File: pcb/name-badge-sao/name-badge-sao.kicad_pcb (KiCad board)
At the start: 2 copper layers, 83.8 x 44.5 mm, 109 parts, among them J1 USB_C_Receptacle_USB2.0, J2 Conn_01x02, SW1 SW_SPDT, U1 IS31FL3731-QF, U2 SAMD21_MOD, U3 W25Q32JVSS, U4 TP4057

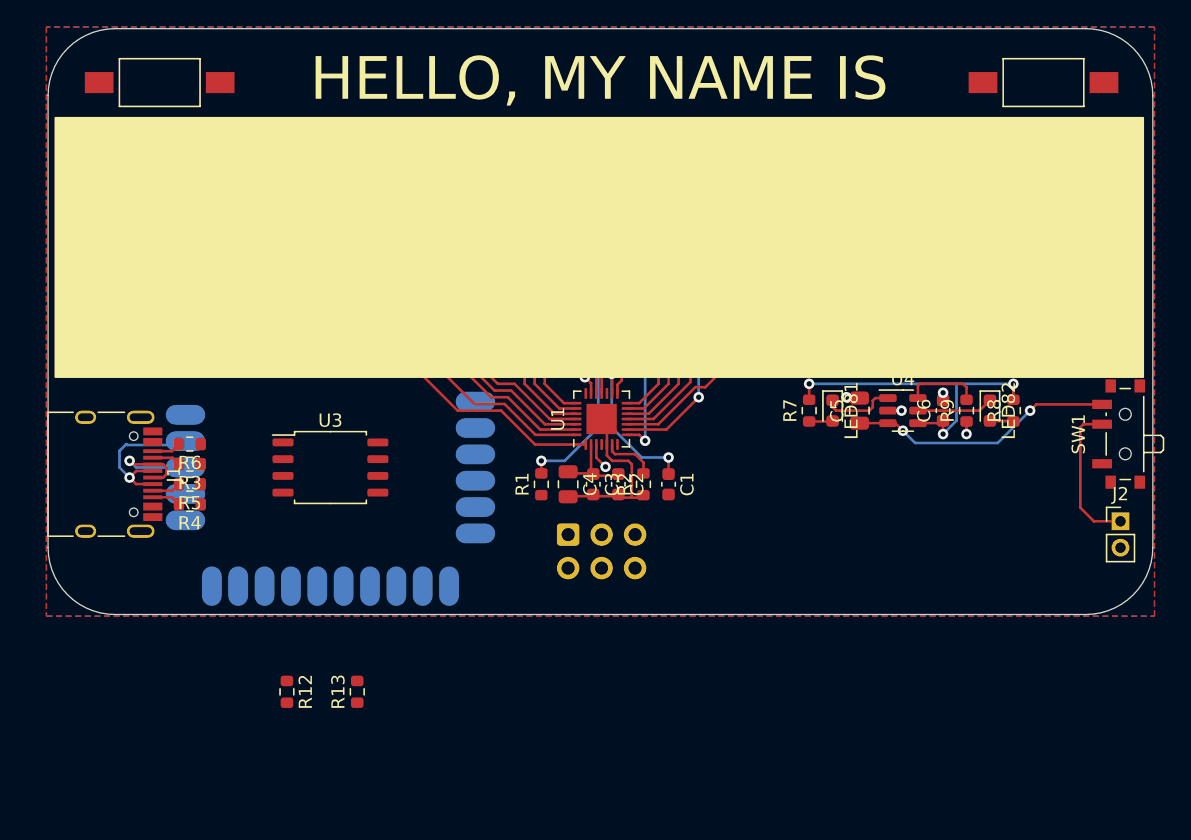
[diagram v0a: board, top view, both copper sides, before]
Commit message: Moving to an all-new circuit design (normal matrix, no charlieplexing) with a new MCU, because why not change everything?
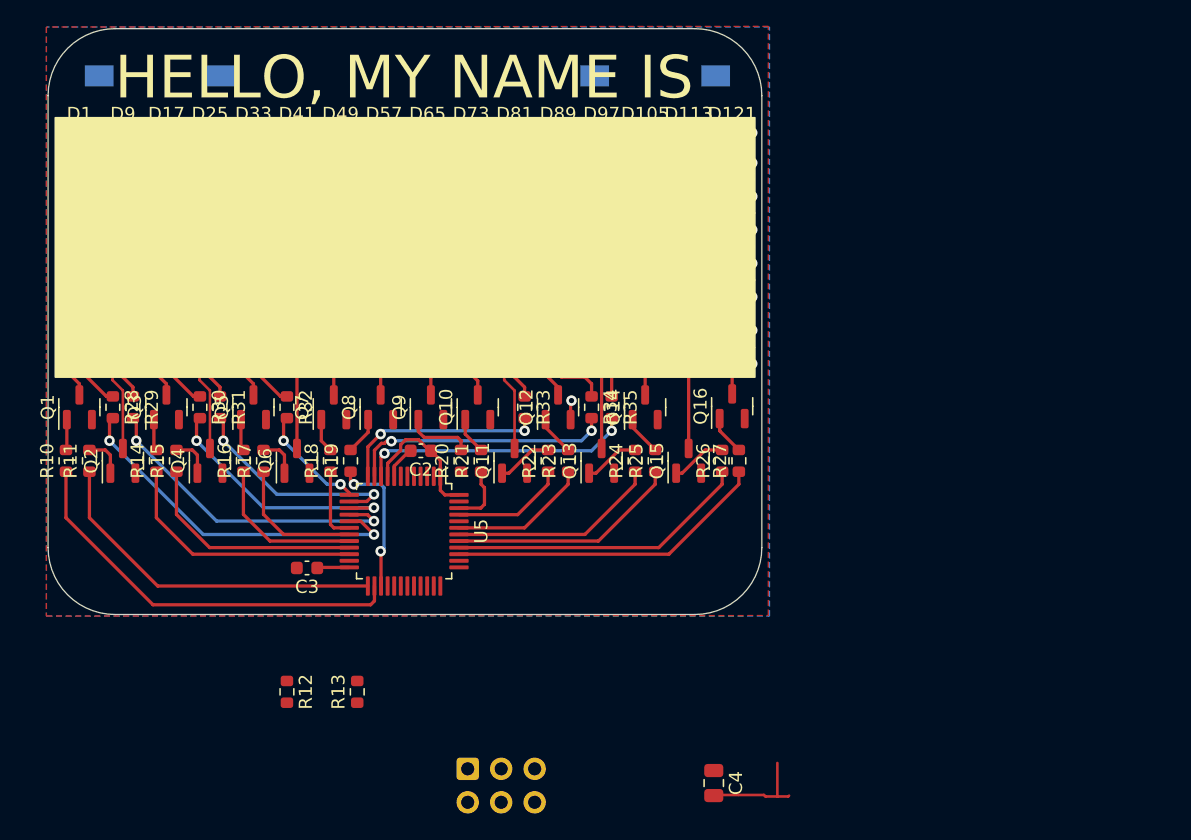
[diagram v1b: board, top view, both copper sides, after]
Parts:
- removed C1: 100n, Capacitor_SMD:C_0603_1608Metric
- removed C5: 10u, Capacitor_SMD:C_0805_2012Metric
- removed C6: 1u, Capacitor_SMD:C_0603_1608Metric
- removed J1: USB_C_Receptacle_USB2.0, Connector_USB:USB_C_Receptacle_HRO_TYPE-C-31-M-12
- removed J2: Conn_01x02, Connector_PinHeader_2.00mm:PinHeader_1x02_P2.00mm_Vertical
- removed LED1, LED10, LED11, LED12, LED13, LED14, LED15, LED16, LED17, LED18, LED19, LED2, LED20, LED21, LED22, LED23, LED24, LED25, LED26, LED27, LED28, LED29, LED3, LED30, LED31, LED32, LED33, LED34, LED35, LED36, LED37, LED38, LED39, LED4, LED40, LED41, LED42, LED43, LED44, LED45, LED46, LED47, LED48, LED49, LED5, LED50, LED51, LED52, LED53, LED54, LED55, LED56, LED57, LED58, LED59, LED6, LED60, LED61, LED62, LED63, LED64, LED65, LED66, LED67, LED68, LED69, LED7, LED70, LED71, LED72, LED73, LED74, LED75, LED76, LED77, LED78, LED79, LED8, LED80, LED81, LED82, LED9: LED, LED_SMD:LED_0603_1608Metric
- removed R1, R2, R9: 10K, Resistor_SMD:R_0603_1608Metric
- removed R3, R4: 5.1K, Resistor_SMD:R_0603_1608Metric
- removed R5, R6: DNP, Resistor_SMD:R_0603_1608Metric
- removed R7, R8: 1K, Resistor_SMD:R_0603_1608Metric
- removed SW1: SW_SPDT, Button_Switch_SMD:SW_SPDT_PCM12
- removed U1: IS31FL3731-QF, Package_DFN_QFN:QFN-28-1EP_4x4mm_P0.4mm_EP2.3x2.3mm
- removed U2: SAMD21_MOD, hcc_mod:SAMD_HCC_G_FOOT
- removed U3: W25Q32JVSS, Package_SO:SOIC-8_5.23x5.23mm_P1.27mm
- removed U4: TP4057, Package_TO_SOT_SMD:SOT-23-6
- added D1: LED, LED_SMD:LED_0603_1608Metric, F.Cu at (109.0, 90.7)
- added D10: LED, LED_SMD:LED_0603_1608Metric, F.Cu at (112.3, 93.0)
- added D100: LED, LED_SMD:LED_0603_1608Metric, F.Cu at (148.6, 98.0)
- added D101: LED, LED_SMD:LED_0603_1608Metric, F.Cu at (148.6, 100.6)
- added D102: LED, LED_SMD:LED_0603_1608Metric, F.Cu at (148.6, 103.1)
- added D103: LED, LED_SMD:LED_0603_1608Metric, F.Cu at (148.6, 105.7)
- added D104: LED, LED_SMD:LED_0603_1608Metric, F.Cu at (148.6, 108.2)
- added D105: LED, LED_SMD:LED_0603_1608Metric, F.Cu at (151.9, 90.7)
- added D106: LED, LED_SMD:LED_0603_1608Metric, F.Cu at (151.9, 93.0)
- added D107: LED, LED_SMD:LED_0603_1608Metric, F.Cu at (151.9, 95.5)
- added D108: LED, LED_SMD:LED_0603_1608Metric, F.Cu at (151.9, 98.0)
- added D109: LED, LED_SMD:LED_0603_1608Metric, F.Cu at (151.9, 100.6)
- added D11: LED, LED_SMD:LED_0603_1608Metric, F.Cu at (112.3, 95.5)
- added D110: LED, LED_SMD:LED_0603_1608Metric, F.Cu at (151.9, 103.1)
- added D111: LED, LED_SMD:LED_0603_1608Metric, F.Cu at (151.9, 105.7)
- added D112: LED, LED_SMD:LED_0603_1608Metric, F.Cu at (151.9, 108.2)
- added D113: LED, LED_SMD:LED_0603_1608Metric, F.Cu at (155.2, 90.7)
- added D114: LED, LED_SMD:LED_0603_1608Metric, F.Cu at (155.2, 93.0)
- added D115: LED, LED_SMD:LED_0603_1608Metric, F.Cu at (155.2, 95.5)
- added D116: LED, LED_SMD:LED_0603_1608Metric, F.Cu at (155.2, 98.0)
- added D117: LED, LED_SMD:LED_0603_1608Metric, F.Cu at (155.2, 100.6)
- added D118: LED, LED_SMD:LED_0603_1608Metric, F.Cu at (155.2, 103.1)
- added D119: LED, LED_SMD:LED_0603_1608Metric, F.Cu at (155.2, 105.7)
- added D12: LED, LED_SMD:LED_0603_1608Metric, F.Cu at (112.3, 98.0)
- added D120: LED, LED_SMD:LED_0603_1608Metric, F.Cu at (155.2, 108.2)
- added D121: LED, LED_SMD:LED_0603_1608Metric, F.Cu at (158.5, 90.7)
- added D122: LED, LED_SMD:LED_0603_1608Metric, F.Cu at (158.5, 93.0)
- added D123: LED, LED_SMD:LED_0603_1608Metric, F.Cu at (158.5, 95.5)
- added D124: LED, LED_SMD:LED_0603_1608Metric, F.Cu at (158.5, 98.0)
- added D125: LED, LED_SMD:LED_0603_1608Metric, F.Cu at (158.5, 100.6)
- added D126: LED, LED_SMD:LED_0603_1608Metric, F.Cu at (158.5, 103.1)
- added D127: LED, LED_SMD:LED_0603_1608Metric, F.Cu at (158.5, 105.7)
- added D128: LED, LED_SMD:LED_0603_1608Metric, F.Cu at (158.5, 108.2)
- added D13: LED, LED_SMD:LED_0603_1608Metric, F.Cu at (112.3, 100.6)
- added D14: LED, LED_SMD:LED_0603_1608Metric, F.Cu at (112.3, 103.1)
- added D15: LED, LED_SMD:LED_0603_1608Metric, F.Cu at (112.3, 105.7)
- added D16: LED, LED_SMD:LED_0603_1608Metric, F.Cu at (112.3, 108.2)
- added D17: LED, LED_SMD:LED_0603_1608Metric, F.Cu at (115.6, 90.7)
- added D18: LED, LED_SMD:LED_0603_1608Metric, F.Cu at (115.6, 93.0)
- added D19: LED, LED_SMD:LED_0603_1608Metric, F.Cu at (115.6, 95.5)
- added D2: LED, LED_SMD:LED_0603_1608Metric, F.Cu at (109.0, 93.0)
- added D20: LED, LED_SMD:LED_0603_1608Metric, F.Cu at (115.6, 98.0)
- added D21: LED, LED_SMD:LED_0603_1608Metric, F.Cu at (115.6, 100.6)
- added D22: LED, LED_SMD:LED_0603_1608Metric, F.Cu at (115.6, 103.1)
- added D23: LED, LED_SMD:LED_0603_1608Metric, F.Cu at (115.6, 105.7)
- added D24: LED, LED_SMD:LED_0603_1608Metric, F.Cu at (115.6, 108.2)
- added D25: LED, LED_SMD:LED_0603_1608Metric, F.Cu at (118.9, 90.7)
- added D26: LED, LED_SMD:LED_0603_1608Metric, F.Cu at (118.9, 93.0)
- added D27: LED, LED_SMD:LED_0603_1608Metric, F.Cu at (118.9, 95.5)
- added D28: LED, LED_SMD:LED_0603_1608Metric, F.Cu at (118.9, 98.0)
- added D29: LED, LED_SMD:LED_0603_1608Metric, F.Cu at (118.9, 100.6)
- added D3: LED, LED_SMD:LED_0603_1608Metric, F.Cu at (109.0, 95.5)
- added D30: LED, LED_SMD:LED_0603_1608Metric, F.Cu at (118.9, 103.1)
- added D31: LED, LED_SMD:LED_0603_1608Metric, F.Cu at (118.9, 105.7)
- added D32: LED, LED_SMD:LED_0603_1608Metric, F.Cu at (118.9, 108.2)
- added D33: LED, LED_SMD:LED_0603_1608Metric, F.Cu at (122.2, 90.7)
- added D34: LED, LED_SMD:LED_0603_1608Metric, F.Cu at (122.2, 93.0)
- added D35: LED, LED_SMD:LED_0603_1608Metric, F.Cu at (122.2, 95.5)
- added D36: LED, LED_SMD:LED_0603_1608Metric, F.Cu at (122.2, 98.0)
- added D37: LED, LED_SMD:LED_0603_1608Metric, F.Cu at (122.2, 100.6)
- added D38: LED, LED_SMD:LED_0603_1608Metric, F.Cu at (122.2, 103.1)
- added D39: LED, LED_SMD:LED_0603_1608Metric, F.Cu at (122.2, 105.7)
- added D4: LED, LED_SMD:LED_0603_1608Metric, F.Cu at (109.0, 98.0)
- added D40: LED, LED_SMD:LED_0603_1608Metric, F.Cu at (122.2, 108.2)
- added D41: LED, LED_SMD:LED_0603_1608Metric, F.Cu at (125.5, 90.7)
- added D42: LED, LED_SMD:LED_0603_1608Metric, F.Cu at (125.5, 93.0)
- added D43: LED, LED_SMD:LED_0603_1608Metric, F.Cu at (125.5, 95.5)
- added D44: LED, LED_SMD:LED_0603_1608Metric, F.Cu at (125.5, 98.0)
- added D45: LED, LED_SMD:LED_0603_1608Metric, F.Cu at (125.5, 100.6)
- added D46: LED, LED_SMD:LED_0603_1608Metric, F.Cu at (125.5, 103.1)
- added D47: LED, LED_SMD:LED_0603_1608Metric, F.Cu at (125.5, 105.7)
- added D48: LED, LED_SMD:LED_0603_1608Metric, F.Cu at (125.5, 108.2)
- added D49: LED, LED_SMD:LED_0603_1608Metric, F.Cu at (128.8, 90.7)
- added D5: LED, LED_SMD:LED_0603_1608Metric, F.Cu at (109.0, 100.6)
- added D50: LED, LED_SMD:LED_0603_1608Metric, F.Cu at (128.8, 93.0)
- added D51: LED, LED_SMD:LED_0603_1608Metric, F.Cu at (128.8, 95.5)
- added D52: LED, LED_SMD:LED_0603_1608Metric, F.Cu at (128.8, 98.0)
- added D53: LED, LED_SMD:LED_0603_1608Metric, F.Cu at (128.8, 100.6)
- added D54: LED, LED_SMD:LED_0603_1608Metric, F.Cu at (128.8, 103.1)
- added D55: LED, LED_SMD:LED_0603_1608Metric, F.Cu at (128.8, 105.7)
- added D56: LED, LED_SMD:LED_0603_1608Metric, F.Cu at (128.8, 108.2)
- added D57: LED, LED_SMD:LED_0603_1608Metric, F.Cu at (132.1, 90.7)
- added D58: LED, LED_SMD:LED_0603_1608Metric, F.Cu at (132.1, 93.0)
- added D59: LED, LED_SMD:LED_0603_1608Metric, F.Cu at (132.1, 95.5)
- added D6: LED, LED_SMD:LED_0603_1608Metric, F.Cu at (109.0, 103.1)
- added D60: LED, LED_SMD:LED_0603_1608Metric, F.Cu at (132.1, 98.0)
- added D61: LED, LED_SMD:LED_0603_1608Metric, F.Cu at (132.1, 100.6)
- added D62: LED, LED_SMD:LED_0603_1608Metric, F.Cu at (132.1, 103.1)
- added D63: LED, LED_SMD:LED_0603_1608Metric, F.Cu at (132.1, 105.7)
- added D64: LED, LED_SMD:LED_0603_1608Metric, F.Cu at (132.1, 108.2)
- added D65: LED, LED_SMD:LED_0603_1608Metric, F.Cu at (135.4, 90.7)
- added D66: LED, LED_SMD:LED_0603_1608Metric, F.Cu at (135.4, 93.0)
- added D67: LED, LED_SMD:LED_0603_1608Metric, F.Cu at (135.4, 95.5)
- added D68: LED, LED_SMD:LED_0603_1608Metric, F.Cu at (135.4, 98.0)
- added D69: LED, LED_SMD:LED_0603_1608Metric, F.Cu at (135.4, 100.6)
- added D7: LED, LED_SMD:LED_0603_1608Metric, F.Cu at (109.0, 105.7)
- added D70: LED, LED_SMD:LED_0603_1608Metric, F.Cu at (135.4, 103.1)
- added D71: LED, LED_SMD:LED_0603_1608Metric, F.Cu at (135.4, 105.7)
- added D72: LED, LED_SMD:LED_0603_1608Metric, F.Cu at (135.4, 108.2)
- added D73: LED, LED_SMD:LED_0603_1608Metric, F.Cu at (138.7, 90.7)
- added D74: LED, LED_SMD:LED_0603_1608Metric, F.Cu at (138.7, 93.0)
- added D75: LED, LED_SMD:LED_0603_1608Metric, F.Cu at (138.7, 95.5)
- added D76: LED, LED_SMD:LED_0603_1608Metric, F.Cu at (138.7, 98.0)
- added D77: LED, LED_SMD:LED_0603_1608Metric, F.Cu at (138.7, 100.6)
- added D78: LED, LED_SMD:LED_0603_1608Metric, F.Cu at (138.7, 103.1)
- added D79: LED, LED_SMD:LED_0603_1608Metric, F.Cu at (138.7, 105.7)
- added D8: LED, LED_SMD:LED_0603_1608Metric, F.Cu at (109.0, 108.2)
- added D80: LED, LED_SMD:LED_0603_1608Metric, F.Cu at (138.7, 108.2)
- added D81: LED, LED_SMD:LED_0603_1608Metric, F.Cu at (142.0, 90.7)
- added D82: LED, LED_SMD:LED_0603_1608Metric, F.Cu at (142.0, 93.0)
- added D83: LED, LED_SMD:LED_0603_1608Metric, F.Cu at (142.0, 95.5)
- added D84: LED, LED_SMD:LED_0603_1608Metric, F.Cu at (142.0, 98.0)
- added D85: LED, LED_SMD:LED_0603_1608Metric, F.Cu at (142.0, 100.6)
- added D86: LED, LED_SMD:LED_0603_1608Metric, F.Cu at (142.0, 103.1)
- added D87: LED, LED_SMD:LED_0603_1608Metric, F.Cu at (142.0, 105.7)
- added D88: LED, LED_SMD:LED_0603_1608Metric, F.Cu at (142.0, 108.2)
- added D89: LED, LED_SMD:LED_0603_1608Metric, F.Cu at (145.3, 90.7)
- added D9: LED, LED_SMD:LED_0603_1608Metric, F.Cu at (112.3, 90.7)
- added D90: LED, LED_SMD:LED_0603_1608Metric, F.Cu at (145.3, 93.0)
- added D91: LED, LED_SMD:LED_0603_1608Metric, F.Cu at (145.3, 95.5)
- added D92: LED, LED_SMD:LED_0603_1608Metric, F.Cu at (145.3, 98.0)
- added D93: LED, LED_SMD:LED_0603_1608Metric, F.Cu at (145.3, 100.6)
- added D94: LED, LED_SMD:LED_0603_1608Metric, F.Cu at (145.3, 103.1)
- added D95: LED, LED_SMD:LED_0603_1608Metric, F.Cu at (145.3, 105.7)
- added D96: LED, LED_SMD:LED_0603_1608Metric, F.Cu at (145.3, 108.2)
- added D97: LED, LED_SMD:LED_0603_1608Metric, F.Cu at (148.6, 90.7)
- added D98: LED, LED_SMD:LED_0603_1608Metric, F.Cu at (148.6, 93.0)
- added D99: LED, LED_SMD:LED_0603_1608Metric, F.Cu at (148.6, 95.5)
- added Q1: MMBT3904, Package_TO_SOT_SMD:SOT-23, F.Cu at (109.0, 111.5)
- added Q10: MMBT3904, Package_TO_SOT_SMD:SOT-23, F.Cu at (139.2, 111.5)
- added Q11: MMBT3904, Package_TO_SOT_SMD:SOT-23, F.Cu at (142.0, 115.6)
- added Q12: MMBT3904, Package_TO_SOT_SMD:SOT-23, F.Cu at (145.3, 111.5)
- added Q13: MMBT3904, Package_TO_SOT_SMD:SOT-23, F.Cu at (148.6, 115.6)
- added Q14: MMBT3904, Package_TO_SOT_SMD:SOT-23, F.Cu at (151.9, 111.5)
- added Q15: MMBT3904, Package_TO_SOT_SMD:SOT-23, F.Cu at (155.2, 115.6)
- added Q16: MMBT3904, Package_TO_SOT_SMD:SOT-23, F.Cu at (158.5, 111.4)
- added Q2: MMBT3904, Package_TO_SOT_SMD:SOT-23, F.Cu at (112.3, 115.6)
- added Q3: MMBT3904, Package_TO_SOT_SMD:SOT-23, F.Cu at (115.6, 111.5)
- added Q4: MMBT3904, Package_TO_SOT_SMD:SOT-23, F.Cu at (118.9, 115.6)
- added Q5: MMBT3904, Package_TO_SOT_SMD:SOT-23, F.Cu at (122.2, 111.5)
- added Q6: MMBT3904, Package_TO_SOT_SMD:SOT-23, F.Cu at (125.5, 115.6)
- added Q7: MMBT3904, Package_TO_SOT_SMD:SOT-23, F.Cu at (128.3, 111.5)
- added Q8: MMBT3904, Package_TO_SOT_SMD:SOT-23, F.Cu at (131.8, 111.5)
- added Q9: MMBT3904, Package_TO_SOT_SMD:SOT-23, F.Cu at (135.6, 111.5)
- added R10: 1K, Resistor_SMD:R_0603_1608Metric, F.Cu at (108.0, 115.6)
- added R11: 1K, Resistor_SMD:R_0603_1608Metric, F.Cu at (109.7, 115.6)
- added R14: 1K, Resistor_SMD:R_0603_1608Metric, F.Cu at (114.8, 115.6)
- added R15: 1K, Resistor_SMD:R_0603_1608Metric, F.Cu at (116.3, 115.6)
- added R16: 1K, Resistor_SMD:R_0603_1608Metric, F.Cu at (121.4, 115.6)
- added R17: 1K, Resistor_SMD:R_0603_1608Metric, F.Cu at (122.9, 115.6)
- added R18: 1K, Resistor_SMD:R_0603_1608Metric, F.Cu at (128.0, 115.6)
- added R19: 1K, Resistor_SMD:R_0603_1608Metric, F.Cu at (129.5, 115.6)
- added R20: 1K, Resistor_SMD:R_0603_1608Metric, F.Cu at (137.9, 115.6)
- added R21: 1K, Resistor_SMD:R_0603_1608Metric, F.Cu at (139.4, 115.6)
- added R22: 1K, Resistor_SMD:R_0603_1608Metric, F.Cu at (144.5, 115.6)
- added R23: 1K, Resistor_SMD:R_0603_1608Metric, F.Cu at (146.1, 115.6)
- added R24: 1K, Resistor_SMD:R_0603_1608Metric, F.Cu at (151.1, 115.6)
- added R25: 1K, Resistor_SMD:R_0603_1608Metric, F.Cu at (152.7, 115.6)
- added R26: 1K, Resistor_SMD:R_0603_1608Metric, F.Cu at (157.7, 115.6)
- added R27: 1K, Resistor_SMD:R_0603_1608Metric, F.Cu at (159.0, 115.6)
- added R28: 100, Resistor_SMD:R_0603_1608Metric, F.Cu at (111.5, 111.5)
- added R29: 100, Resistor_SMD:R_0603_1608Metric, F.Cu at (113.0, 111.5)
- added R30: 100, Resistor_SMD:R_0603_1608Metric, F.Cu at (118.1, 111.5)
- added R31: 100, Resistor_SMD:R_0603_1608Metric, F.Cu at (119.6, 111.5)
- added R32: 100, Resistor_SMD:R_0603_1608Metric, F.Cu at (124.7, 111.5)
- added R33: 100, Resistor_SMD:R_0603_1608Metric, F.Cu at (142.7, 111.5)
- added R34: 100, Resistor_SMD:R_0603_1608Metric, F.Cu at (147.8, 111.5)
- added R35: 100, Resistor_SMD:R_0603_1608Metric, F.Cu at (149.4, 111.5)
- added U5: STM32F030C8Tx, Package_QFP:LQFP-48_7x7mm_P0.5mm, F.Cu at (133.6, 120.9)
- S1, S2: moved to B.Cu
- moved S1 67.1 mm to (115.1, 86.4), turned to 0 degrees
- moved S2 37.6 mm to (152.7, 86.4)
- moved C4 25.2 mm to (157.1, 140.0)
- moved C3 22.6 mm to (126.2, 123.7), turned to 180 degrees
- moved SAO1 19.3 mm to (138.4, 138.9)
- moved C2 15.2 mm to (134.9, 114.8), turned to 180 degrees
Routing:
- net /CA9: track 91.9 -> 0.00 mm
- net /CA8: track 88.7 -> 0.00 mm, vias 10 -> 0
- net Net-(D1-A): track 0.00 -> 82.9 mm, vias 0 -> 16
- net /CA5: track 81.0 -> 0.00 mm, vias 9 -> 0
- net /CA6: track 80.5 -> 0.00 mm, vias 10 -> 0
- net /CB9: track 80.1 -> 0.00 mm
- net Net-(D10-A): track 0.00 -> 79.6 mm, vias 0 -> 16
- net Net-(D107-A): track 0.00 -> 78.1 mm, vias 0 -> 16
- net /CB8: track 77.3 -> 0.00 mm, vias 8 -> 0
- net /CB7: track 76.4 -> 0.00 mm, vias 10 -> 0
- net Net-(D100-A): track 0.00 -> 74.6 mm, vias 0 -> 16
- net /CA7: track 73.1 -> 0.00 mm, vias 9 -> 0
- net Net-(D101-A): track 0.00 -> 73.0 mm, vias 0 -> 16
- net /CB6: track 73.0 -> 0.00 mm, vias 10 -> 0
- net Net-(D102-A): track 0.00 -> 69.5 mm, vias 0 -> 16
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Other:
- board size 83.8 x 44.5 mm -> 54.2 x 44.5 mm
- board text added: "JLCJLCJLCJLC"
- board text removed: "LED10"
- board text removed: "LED11"
- board text removed: "LED12"
- board text removed: "LED13"
- board text removed: "LED14"
- board text removed: "LED15"
- board text removed: "LED16"
- board text removed: "LED17"
- board text removed: "LED18"
- board text removed: "LED19"
- board text removed: "LED20"
- board text removed: "LED21"
- board text removed: "LED22"
- board text removed: "LED23"
- board text removed: "LED24"
- board text removed: "LED25"
- board text removed: "LED26"
- board text removed: "LED27"
- board text removed: "LED28"
- board text removed: "LED29"
- board text removed: "LED30"
- board text removed: "LED31"
- board text removed: "LED32"
- board text removed: "LED33"
- board text removed: "LED34"
- board text removed: "LED35"
- board text removed: "LED36"
- board text removed: "LED37"
- board text removed: "LED38"
- board text removed: "LED39"
- board text removed: "LED40"
- board text removed: "LED41"
- board text removed: "LED42"
- board text removed: "LED43"
- board text removed: "LED44"
- board text removed: "LED45"
- board text removed: "LED46"
- board text removed: "LED47"
- board text removed: "LED48"
- board text removed: "LED49"
- board text removed: "LED50"
- board text removed: "LED51"
- board text removed: "LED52"
- board text removed: "LED53"
- board text removed: "LED54"
- board text removed: "LED55"
- board text removed: "LED56"
- board text removed: "LED57"
- board text removed: "LED58"
- board text removed: "LED59"
- board text removed: "LED6"
- board text removed: "LED60"
- board text removed: "LED61"
- board text removed: "LED62"
- board text removed: "LED63"
- board text removed: "LED64"
- board text removed: "LED65"
- board text removed: "LED66"
- board text removed: "LED67"
- board text removed: "LED68"
- board text removed: "LED69"
- board text removed: "LED7"
- board text removed: "LED70"
- board text removed: "LED71"
- board text removed: "LED72"
- board text removed: "LED73"
- board text removed: "LED74"
- board text removed: "LED75"
- board text removed: "LED76"
- board text removed: "LED77"
- board text removed: "LED78"
- board text removed: "LED79"
- board text removed: "LED8"
- board text removed: "LED80"
- board text removed: "LED9"

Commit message: I think that's an SAO
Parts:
- removed SAO1: AVR-ISP-6SMD, Connector_IDC:IDC-Header_2x03_P2.54mm_Vertical
- added J1: Conn_02x03_Odd_Even, Connector_IDC:IDC-Header_2x03_P2.54mm_Vertical_SMD, B.Cu at (133.6, 120.7)
- added J2: BOOT0, TestPoint:TestPoint_Pad_1.5x1.5mm, B.Cu at (143.3, 120.1)
- added J3: RESET, TestPoint:TestPoint_Pad_1.5x1.5mm, B.Cu at (141.0, 110.5)
- added J4: SWDIO, TestPoint:TestPoint_Pad_1.5x1.5mm, B.Cu at (146.1, 124.2)
- added J5: SWCLK, TestPoint:TestPoint_Pad_1.5x1.5mm, B.Cu at (143.3, 124.2)
- added R1: 10K, Resistor_SMD:R_0603_1608Metric, B.Cu at (146.3, 120.1)
- C4, R12, R13: moved to B.Cu
- moved R13 49.2 mm to (152.7, 89.4), turned to 180 degrees
- moved R12 44.7 mm to (115.1, 89.4), turned to 180 degrees
- moved C4 39.3 mm to (129.8, 111.8), turned to 90 degrees
- moved C3 0.36 mm to (126.0, 124.0)
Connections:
- R13 pad 1: /RESET -> /~{RESET}
- S2 pad 2: /RESET -> /~{RESET}
- U5 pad 29: unconnected-(U5-PA8-Pad29) -> /BUTTON
- U5 pad 30: unconnected-(U5-PA9-Pad30) -> /UART_RX
- U5 pad 31: unconnected-(U5-PA10-Pad31) -> /UART_TX
- U5 pad 44: unconnected-(U5-BOOT0-Pad44) -> Net-(J2-Pin_1)
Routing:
- net +3V3: track 12.9 -> 99.3 mm, vias 0 -> 4
- net /BUTTON: track 0.00 -> 71.1 mm, vias 0 -> 1
- net /~{RESET}: track 0.00 -> 67.6 mm, vias 0 -> 4
- net /SWDIO: track 0.00 -> 13.5 mm, vias 0 -> 1
- net /COL8: track 0.00 -> 12.0 mm, vias 0 -> 2
- net /UART_RX: track 0.00 -> 9.97 mm, vias 0 -> 1
- net Net-(J2-Pin_1): track 0.00 -> 9.87 mm, vias 0 -> 1
- net /SCL: track 0.00 -> 7.81 mm, vias 0 -> 1
- net /SWCLK: track 0.00 -> 5.72 mm, vias 0 -> 1
- net /UART_TX: track 0.00 -> 3.82 mm, vias 0 -> 1
- net /ROW3: track 17.0 -> 13.3 mm
- net /ROW0: track 27.1 -> 23.4 mm
- net /ROW1: track 24.5 -> 20.7 mm
- net GND: track 12.4 -> 8.82 mm, vias 1 -> 3
- net /ROW2: track 19.3 -> 15.8 mm
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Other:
- board size 54.2 x 44.5 mm -> 54.2 x 44.7 mm
